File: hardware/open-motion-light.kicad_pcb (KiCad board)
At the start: 4 copper layers, 80 x 80 mm, 98 parts, among them J1 TYPE-C-31-M-12, Q1 2N7002, SW1 SW_Push, SW3 SSSS213800, U1 CN3058E, U2 VCNL4020-GS08, U3 MT9284BS6, U4 XYC-PIR224S-S1, U6 CH340X, U7 STM32L051K8Ux

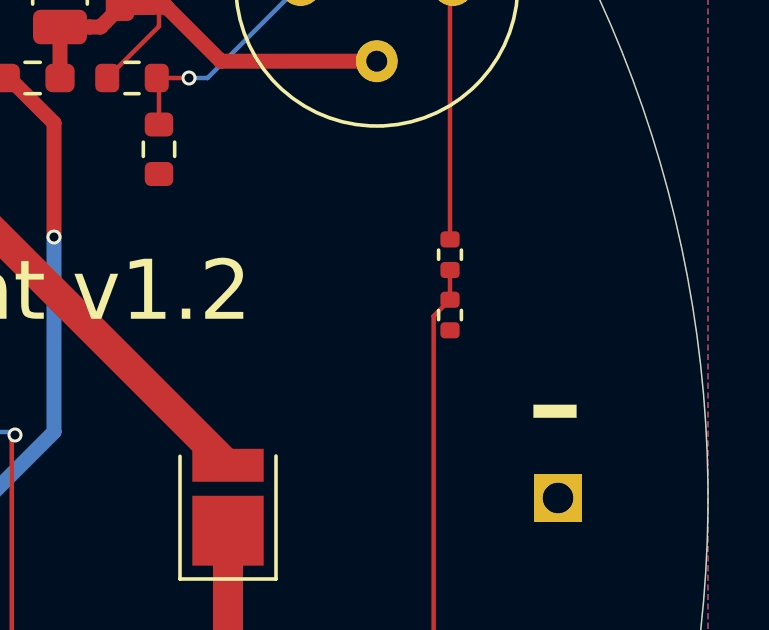
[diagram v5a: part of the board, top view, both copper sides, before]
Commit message: v1.2: remove PIR pulldown
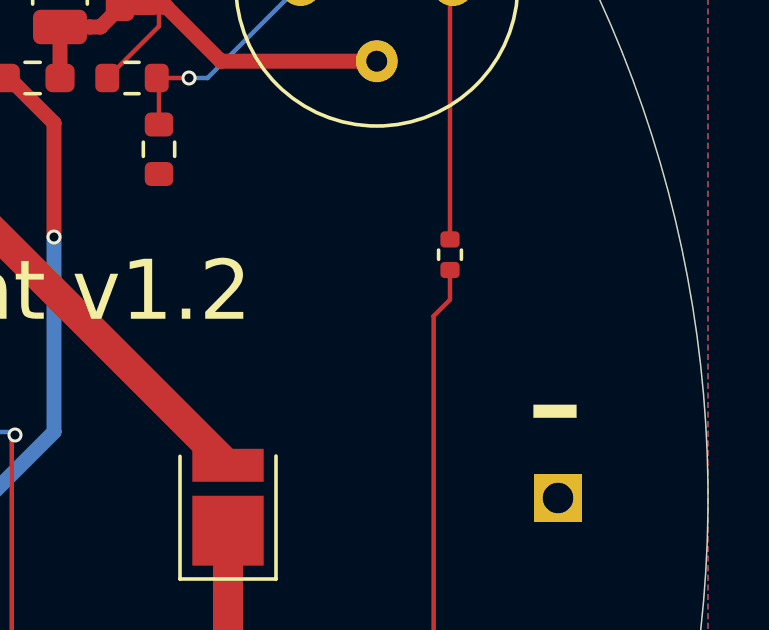
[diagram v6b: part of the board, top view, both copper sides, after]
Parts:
- removed R17: 100k, Resistor_SMD:R_0402_1005Metric
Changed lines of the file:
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@@
 			)
 		)
+		(property "LCSC Part" "C210315"
+			(at 0 0 -150)
+			(unlocked yes)
+			(layer "F.Fab")
+			(hide yes)
+			(effects
+				(font
+					(size 1 1)
+					(thickness 0.15)
+				)
+			)
+		)
+		(property "LCSC" "C210315"
+			(at 0 0 -150)
+			(unlocked yes)
+			(layer "F.Fab")
+			(hide yes)
+			(effects
+				(font
+					(size 1 1)
+					(thickness 0.15)
+				)
+			)
+		)
 		(sheetname "Root")
 		(sheetfile "open-motion-light.kicad_sch")
@@
 	(footprint "Resistor_SMD:R_0402_1005Metric"
 		(layer "F.Cu")
-		(at 119.2 103.8 -90)
-		(descr "Resistor SMD 0402 (1005 Metric), square (rectangular) end terminal, IPC_7351 nominal, (Body size source: IPC-SM-782 page 72, https://www.pcb-3d.com/wordpress/wp-content/uploads/ipc-sm-782a_amendment_1_and_2.pdf), generated with kicad-footprint-generator")
-		(tags "resistor")
-		(property "Reference" "R17"
-			(at 0 -1.17 90)
-			(layer "F.SilkS")
-			(hide yes)
-			(effects
-				(font
-					(size 1 1)
-					(thickness 0.15)
-				)
-			)
-		)
-		(property "Value" "100k"
-			(at 0 1.17 90)
-			(layer "F.Fab")
-			(effects
-				(font
-					(size 1 1)
-					(thickness 0.15)
-				)
-			)
-		)
-		(property "Footprint" "Resistor_SMD:R_0402_1005Metric"
-			(at 0 0 -90)
-			(unlocked yes)
-			(layer "F.Fab")
-			(hide yes)
-			(effects
-				(font
-					(size 1.27 1.27)
-					(thickness 0.15)
-				)
-			)
-		)
-		(property "Datasheet" ""
-			(at 0 0 -90)
-			(unlocked yes)
-			(layer "F.Fab")
-			(hide yes)
-			(effects
-				(font
-					(size 1.27 1.27)
-					(thickness 0.15)
-				)
-			)
-		)
-		(property "Description" "Resistor"
-			(at 0 0 -90)
-			(unlocked yes)
-			(layer "F.Fab")
-			(hide yes)
-			(effects
-				(font
-					(size 1.27 1.27)
-					(thickness 0.15)
-				)
-			)
-		)
-		(property "LCSC" "C25741"
-			(at 0 0 -90)
-			(unlocked yes)
-			(layer "F.Fab")
-			(hide yes)
-			(effects
-				(font
-					(size 1 1)
-					(thickness 0.15)
-				)
-			)
-		)
-		(property ki_fp_filters "R_*")
-		(sheetname "Root")
-		(sheetfile "open-motion-light.kicad_sch")
-		(attr smd)
-		(fp_line
-			(start -0.153641 0.38)
-			(end 0.153641 0.38)
-			(stroke
-				(width 0.12)
-				(type solid)
-			)
-			(layer "F.SilkS")
-		)
-		(fp_line
-			(start -0.153641 -0.38)
-			(end 0.153641 -0.38)
-			(stroke
-				(width 0.12)
-				(type solid)
-			)
-			(layer "F.SilkS")
-		)
-		(fp_line
-			(start -0.93 0.47)
-			(end -0.93 -0.47)
-			(stroke
-				(width 0.05)
-				(type solid)
-			)
-			(layer "F.CrtYd")
-		)
-		(fp_line
-			(start 0.93 0.47)
-			(end -0.93 0.47)
-			(stroke
-				(width 0.05)
-				(type solid)
-			)
-			(layer "F.CrtYd")
-		)
-		(fp_line
-			(start -0.93 -0.47)
-			(end 0.93 -0.47)
-			(stroke
-				(width 0.05)
-				(type solid)
-			)
-			(layer "F.CrtYd")
-		)
-		(fp_line
-			(start 0.93 -0.47)
-			(end 0.93 0.47)
-			(stroke
-				(width 0.05)
-				(type solid)
-			)
-			(layer "F.CrtYd")
-		)
-		(fp_line
-			(start -0.525 0.27)
-			(end -0.525 -0.27)
-			(stroke
-				(width 0.1)
-				(type solid)
-			)
-			(layer "F.Fab")
-		)
-		(fp_line
-			(start 0.525 0.27)
-			(end -0.525 0.27)
-			(stroke
-				(width 0.1)
-				(type solid)
-			)
-			(layer "F.Fab")
-		)
-		(fp_line
-			(start -0.525 -0.27)
-			(end 0.525 -0.27)
-			(stroke
-				(width 0.1)
-				(type solid)
-			)
-			(layer "F.Fab")
-		)
-		(fp_line
-			(start 0.525 -0.27)
-			(end 0.525 0.27)
-			(stroke
-				(width 0.1)
-				(type solid)
-			)
-			(layer "F.Fab")
-		)
-		(fp_text user "${REFERENCE}"
-			(at 0 0 90)
-			(layer "F.Fab")
-			(effects
-				(font
-					(size 0.26 0.26)
-					(thickness 0.04)
-				)
-			)
-		)
-		(pad "1" smd roundrect
-			(at -0.51 0 270)
-			(size 0.54 0.64)
-			(layers "F.Cu" "F.Paste" "F.Mask")
-			(roundrect_rratio 0.25)
-			(net 43 "/PIR")
-			(pintype "passive")
-		)
-		(pad "2" smd roundrect
-			(at 0.51 0 270)
-			(size 0.54 0.64)
-			(layers "F.Cu" "F.Paste" "F.Mask")
-			(roundrect_rratio 0.25)
-			(net 2 "GND")
-			(pintype "passive")
-		)
-		(model "${KICAD8_3DMODEL_DIR}/Resistor_SMD.3dshapes/R_0402_1005Metric.wrl"
-			(offset
-				(xyz 0 0 0)
-			)
-			(scale
-				(xyz 1 1 1)
-			)
-			(rotate
-				(xyz 0 0 0)
-			)
-		)
-	)
-	(footprint "Resistor_SMD:R_0402_1005Metric"
-		(layer "F.Cu")
 		(at 73.7 111 -90)
 		(descr "Resistor SMD 0402 (1005 Metric), square (rectangular) end terminal, IPC_7351 nominal, (Body size source: IPC-SM-782 page 72, https://www.pcb-3d.com/wordpress/wp-content/uploads/ipc-sm-782a_amendment_1_and_2.pdf), generated with kicad-footprint-generator")
@@
 		(tags "resistor")
 		(property "Reference" "R13"
-			(at 0 -1.17 360)
+			(at 0 -1.17 0)
 			(layer "F.SilkS")
 			(hide yes)
@@
 		)
 		(property "Value" "1k"
-			(at 0 1.17 360)
+			(at 0 1.17 0)
 			(layer "F.Fab")
 			(effects
@@
 		)
 		(fp_text user "${REFERENCE}"
-			(at 0 0 360)
+			(at 0 0 0)
 			(layer "F.Fab")
 			(effects
@@
 			)
 		)
+		(property "LCSC Part" "C210315"
+			(at 0 0 -90)
+			(unlocked yes)
+			(layer "F.Fab")
+			(hide yes)
+			(effects
+				(font
+					(size 1 1)
+					(thickness 0.15)
+				)
+			)
+		)
+		(property "LCSC" "C210315"
+			(at 0 0 -90)
+			(unlocked yes)
+			(layer "F.Fab")
+			(hide yes)
+			(effects
+				(font
+					(size 1 1)
+					(thickness 0.15)
+				)
+			)
+		)
 		(sheetname "Root")
 		(sheetfile "open-motion-light.kicad_sch")
@@
 			)
 		)
+		(property "LCSC Part" "C210315"
+			(at 0 0 90)
+			(unlocked yes)
+			(layer "F.Fab")
+			(hide yes)
+			(effects
+				(font
+					(size 1 1)
+					(thickness 0.15)
+				)
+			)
+		)
+		(property "LCSC" "C210315"
+			(at 0 0 90)
+			(unlocked yes)
+			(layer "F.Fab")
+			(hide yes)
+			(effects
+				(font
+					(size 1 1)
+					(thickness 0.15)
+				)
+			)
+		)
 		(sheetname "Root")
 		(sheetfile "open-motion-light.kicad_sch")
@@
 			)
 		)
+		(property "LCSC Part" "C210315"
+			(at 0 0 -30)
+			(unlocked yes)
+			(layer "F.Fab")
+			(hide yes)
+			(effects
+				(font
+					(size 1 1)
+					(thickness 0.15)
+				)
+			)
+		)
+		(property "LCSC" "C210315"
+			(at 0 0 -30)
+			(unlocked yes)
+			(layer "F.Fab")
+			(hide yes)
+			(effects
+				(font
+					(size 1 1)
+					(thickness 0.15)
+				)
+			)
+		)
 		(sheetname "Root")
 		(sheetfile "open-motion-light.kicad_sch")
@@
 			)
 		)
+		(property "LCSC Part" "C210315"
+			(at 0 0 30)
+			(unlocked yes)
+			(layer "F.Fab")
+			(hide yes)
+			(effects
+				(font
+					(size 1 1)
+					(thickness 0.15)
+				)
+			)
+		)
+		(property "LCSC" "C210315"
+			(at 0 0 30)
+			(unlocked yes)
+			(layer "F.Fab")
+			(hide yes)
+			(effects
+				(font
+					(size 1 1)
+					(thickness 0.15)
+				)
+			)
+		)
 		(sheetname "Root")
 		(sheetfile "open-motion-light.kicad_sch")
@@
 			)
 		)
+		(property "LCSC Part" "C210315"
+			(at 0 0 150)
+			(unlocked yes)
+			(layer "F.Fab")
+			(hide yes)
+			(effects
+				(font
+					(size 1 1)
+					(thickness 0.15)
+				)
+			)
+		)
+		(property "LCSC" "C210315"
+			(at 0 0 150)
+			(unlocked yes)
+			(layer "F.Fab")
+			(hide yes)
+			(effects
+				(font
+					(size 1 1)
+					(thickness 0.15)
+				)
+			)
+		)
 		(sheetname "Root")
 		(sheetfile "open-motion-light.kicad_sch")
@@
 		(tags "resistor")
 		(property "Reference" "R42"
-			(at 0 -1.43 360)
+			(at 0 -1.43 0)
 			(layer "F.SilkS")
 			(hide yes)
@@
 		)
 		(property "Value" "330k"
-			(at 0 1.43 360)
+			(at 0 1.43 0)
 			(layer "F.Fab")
 			(effects
@@
 		)
 		(fp_text user "${REFERENCE}"
-			(at 0 0 360)
+			(at 0 0 0)
 			(layer "F.Fab")
 			(effects
@@
 		(tags "resistor")
 		(property "Reference" "R34"
-			(at 0 -1.17 360)
+			(at 0 -1.17 0)
 			(layer "F.SilkS")
 			(hide yes)
@@
 		)
 		(property "Value" "1k"
-			(at 0 1.17 360)
+			(at 0 1.17 0)
 			(layer "F.Fab")
 			(effects
@@
 		)
 		(fp_text user "${REFERENCE}"
-			(at 0 0 360)
+			(at 0 0 0)
 			(layer "F.Fab")
 			(effects

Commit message: Hardware v1.2
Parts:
- added C23: 100nF, Capacitor_SMD:C_0402_1005Metric, F.Cu at (85.1, 124.1)
- added C24: 10uF, Capacitor_SMD:C_0603_1608Metric, F.Cu at (85.5, 122.9)
- C1: value 4.7uF -> 47uF; footprint Capacitor_SMD:C_0603_1608Metric -> Capacitor_SMD:C_1206_3216Metric
- moved C1 5.36 mm to (85.8, 121.0), turned to 0 degrees
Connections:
- C1 pad 1: +5V -> GND
- C1 pad 2: GND -> +5V
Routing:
- net +5V: track 57.7 -> 61.5 mm
- net GND: track 141.2 -> 143.1 mm, vias 75 -> 162
- net /USART_TX: track 42.8 -> 43.4 mm
